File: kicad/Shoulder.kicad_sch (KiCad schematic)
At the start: 9 parts, among them U301 NSP4201MR6

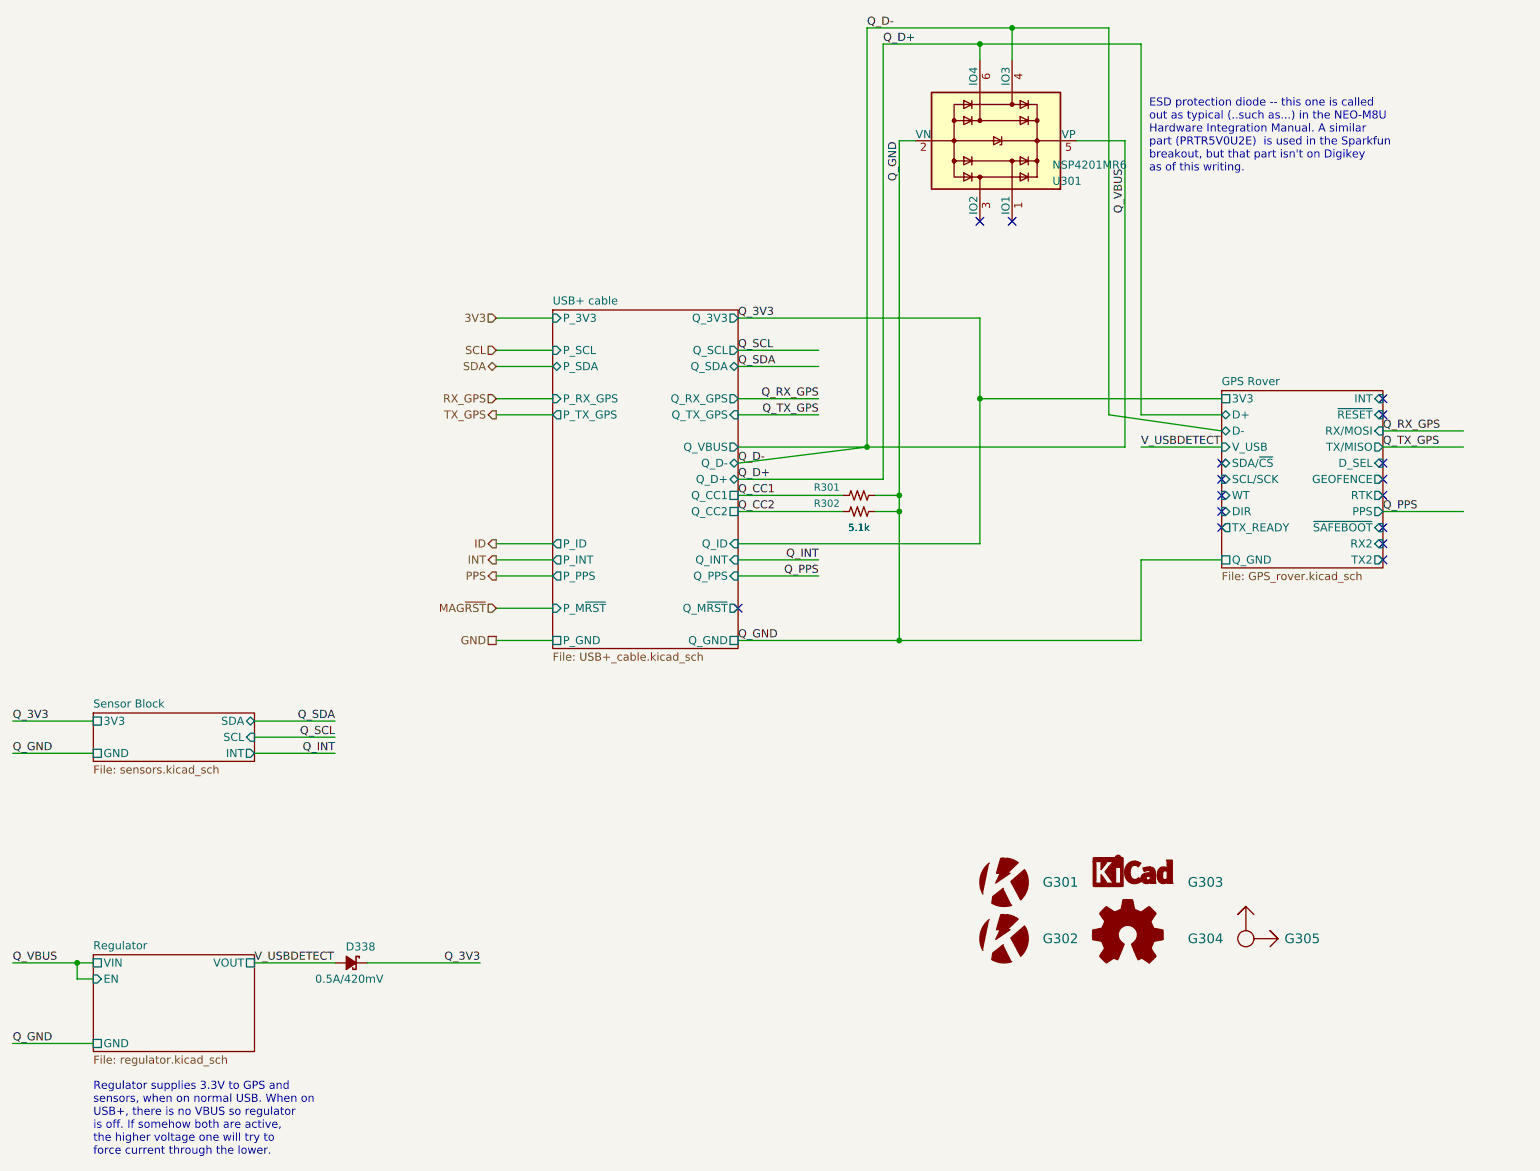
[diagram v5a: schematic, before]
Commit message: Corrected Digikey numbers
Stupid supply chain :( . Updated protection diode for data lines. Removed heirarchical pins which are no longer present in the nested sheet.
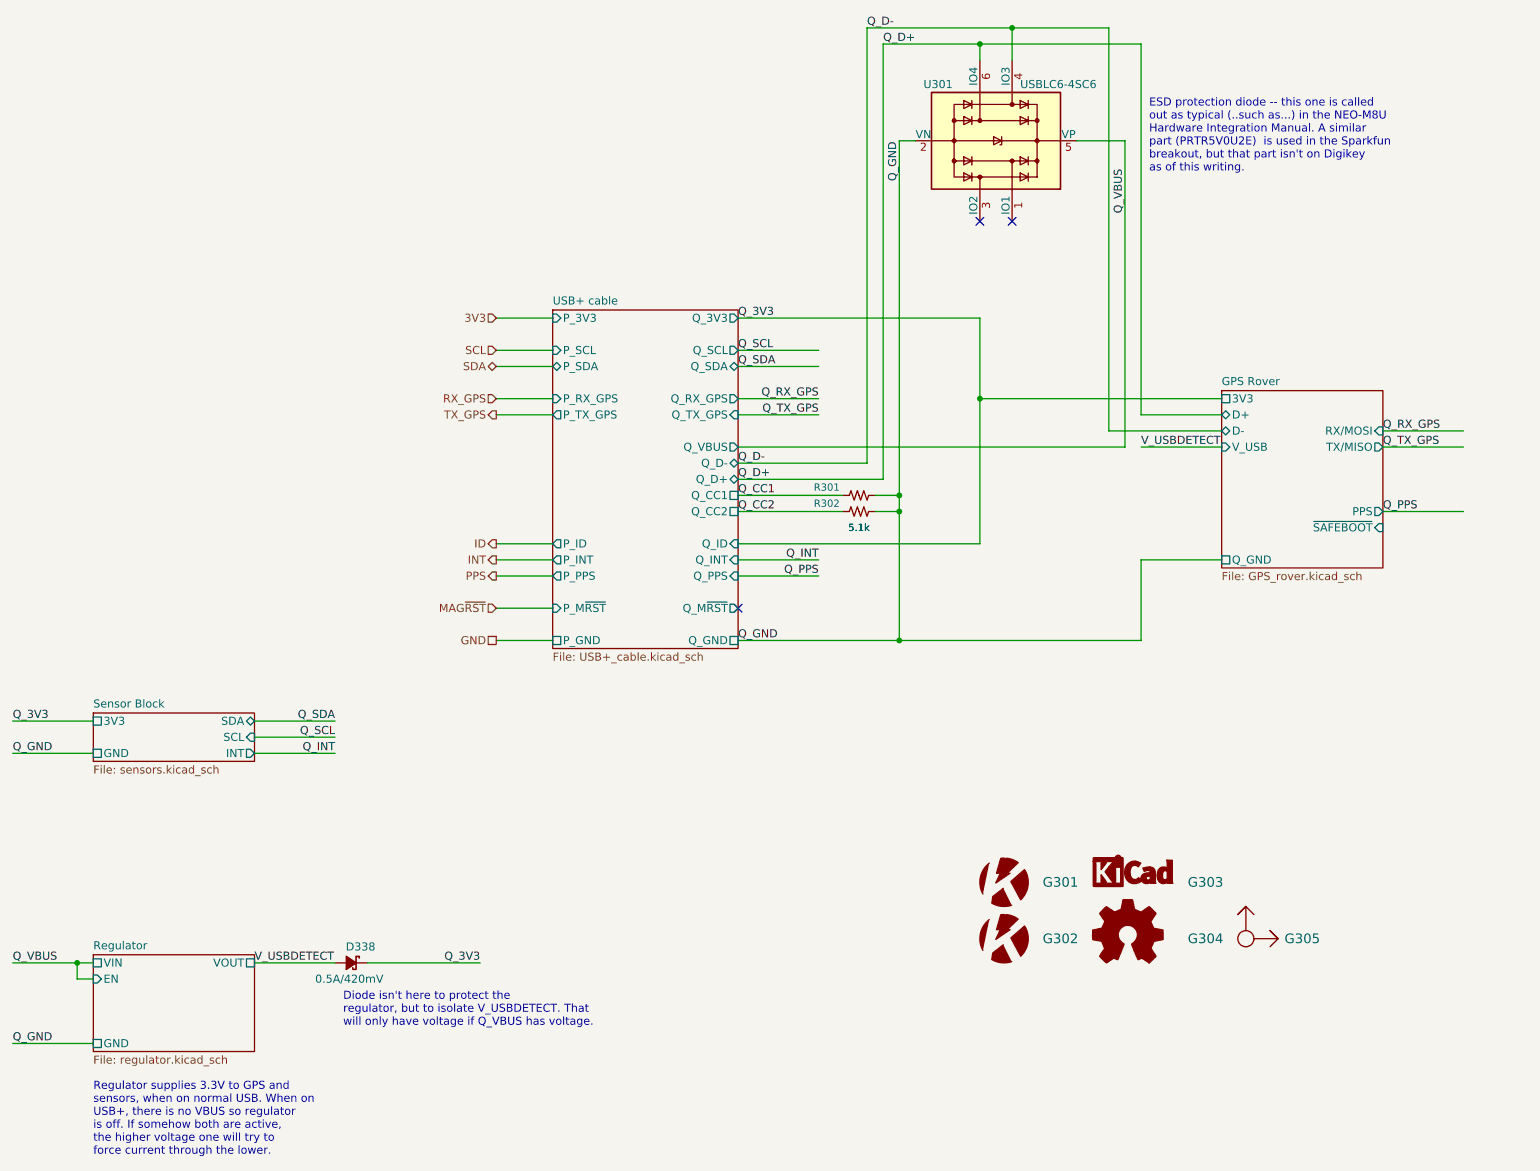
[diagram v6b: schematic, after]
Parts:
- D338: Digikey 641-1520-1-ND -> 641-1332-1-ND
- U301: value NSP4201MR6 -> USBLC6-4SC6; Digikey 497-5235-1-ND -> 497-4492-1-ND; Purpose USB DP protection diodes -> USB data ESD protection diodes
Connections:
- net Q_D-: no longer U301.5 (VP)
- new net Q_VBUS: U301.5 (VP)
- no-connect marks 16 -> 3
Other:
- sheet GPS Rover ports: added none; removed DIR, D_SEL, GEOFENCE, INT, RTK, RX2, SCL/SCK, SDA/~{CS}, TX2, TX_READY, WT, ~{RESET}
- note added: "Diode isn't here to protect the regulator, but to isolate V_USBDETECT. That will only have voltage if Q_VBUS has voltage."
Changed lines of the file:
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@@
   (junction (at 165.1 93.98) (diameter 0) (color 0 0 0 0)
   )
-  (junction (at 160.02 83.82) (diameter 0) (color 0 0 0 0)
-  )
   (junction (at 35.56 165.1) (diameter 0) (color 0 0 0 0)
   )
   (junction (at 165.1 91.44) (diameter 0) (color 0 0 0 0)
   )
-  (no_connect (at 215.9 96.52))
   (no_connect (at 182.88 48.26))
   (no_connect (at 139.7 109.22))
-  (no_connect (at 215.9 93.98))
-  (no_connect (at 215.9 91.44))
-  (no_connect (at 215.9 88.9))
-  (no_connect (at 215.9 86.36))
-  (no_connect (at 241.3 88.9))
-  (no_connect (at 241.3 91.44))
-  (no_connect (at 241.3 96.52))
-  (no_connect (at 241.3 99.06))
-  (no_connect (at 241.3 101.6))
-  (no_connect (at 241.3 86.36))
-  (no_connect (at 241.3 76.2))
-  (no_connect (at 241.3 78.74))
   (no_connect (at 177.8 48.26))
   (wire (pts (xy 241.3 83.82) (xy 254 83.82))
@@
     (stroke (width 0) (type default) (color 0 0 0 0))
   )
-  (wire (pts (xy 215.9 81.28) (xy 198.12 78.74))
+  (wire (pts (xy 198.12 17.78) (xy 198.12 81.28))
     (stroke (width 0) (type default) (color 0 0 0 0))
   )
@@
     (stroke (width 0) (type default) (color 0 0 0 0))
   )
+  (wire (pts (xy 139.7 86.36) (xy 160.02 86.36))
+    (stroke (width 0) (type default) (color 0 0 0 0))
+  )
   (wire (pts (xy 139.7 63.5) (xy 177.8 63.5))
     (stroke (width 0) (type default) (color 0 0 0 0))
   )
+  (wire (pts (xy 160.02 17.78) (xy 160.02 86.36))
+    (stroke (width 0) (type default) (color 0 0 0 0))
+  )
   (wire (pts (xy 177.8 76.2) (xy 215.9 76.2))
     (stroke (width 0) (type default) (color 0 0 0 0))
   )
-  (wire (pts (xy 139.7 83.82) (xy 160.02 83.82))
-    (stroke (width 0) (type default) (color 0 0 0 0))
-  )
   (wire (pts (xy 241.3 93.98) (xy 254 93.98))
     (stroke (width 0) (type default) (color 0 0 0 0))
@@
     (stroke (width 0) (type default) (color 0 0 0 0))
   )
-  (wire (pts (xy 160.02 83.82) (xy 200.66 83.82))
+  (wire (pts (xy 139.7 83.82) (xy 200.66 83.82))
     (stroke (width 0) (type default) (color 0 0 0 0))
   )
@@
     (stroke (width 0) (type default) (color 0 0 0 0))
   )
-  (wire (pts (xy 198.12 78.74) (xy 198.12 17.78))
-    (stroke (width 0) (type default) (color 0 0 0 0))
-  )
   (wire (pts (xy 160.02 17.78) (xy 182.88 17.78))
     (stroke (width 0) (type default) (color 0 0 0 0))
@@
     (stroke (width 0) (type default) (color 0 0 0 0))
   )
-  (wire (pts (xy 160.02 83.82) (xy 160.02 17.78))
-    (stroke (width 0) (type default) (color 0 0 0 0))
-  )
   (wire (pts (xy 203.2 20.32) (xy 203.2 78.74))
     (stroke (width 0) (type default) (color 0 0 0 0))
@@
     (stroke (width 0) (type default) (color 0 0 0 0))
   )
-  (wire (pts (xy 139.7 86.36) (xy 160.02 83.82))
-    (stroke (width 0) (type default) (color 0 0 0 0))
-  )
   (wire (pts (xy 177.8 20.32) (xy 203.2 20.32))
     (stroke (width 0) (type default) (color 0 0 0 0))
@@
   )
   (wire (pts (xy 182.88 17.78) (xy 182.88 22.86))
+    (stroke (width 0) (type default) (color 0 0 0 0))
+  )
+  (wire (pts (xy 215.9 81.28) (xy 198.12 81.28))
     (stroke (width 0) (type default) (color 0 0 0 0))
   )
@@
   (text "ESD protection diode -- this one is called\nout as typical (..such as...) in the NEO-M8U\nHardware Integration Manual. A similar\npart (PRTR5V0U2E)  is used in the Sparkfun\nbreakout, but that part isn't on Digikey\nas of this writing."
     (at 204.47 40.64 0)
+    (effects (font (size 1.27 1.27)) (justify left bottom))
+  )
+  (text "Diode isn't here to protect the\nregulator, but to isolate V_USBDETECT. That\nwill only have voltage if Q_VBUS has voltage."
+    (at 77.47 175.26 0)
     (effects (font (size 1.27 1.27)) (justify left bottom))
   )
@@
       (effects (font (size 1.27 1.27)) hide)
     )
-    (property "Digikey" "641-1520-1-ND" (id 4) (at 78.74 165.1 0)
+    (property "Digikey" "641-1332-1-ND" (id 4) (at 78.74 165.1 0)
       (effects (font (size 1.27 1.27)) hide)
     )
@@
   (symbol (lib_id "Power_Protection:SRV05-4") (at 180.34 35.56 270) (mirror x) (unit 1)
     (in_bom yes) (on_board yes)
-    (property "Reference" "U301" (id 0) (at 189.23 41.91 90)
-      (effects (font (size 1.27 1.27)) (justify left))
-    )
-    (property "Value" "NSP4201MR6" (id 1) (at 189.23 39.37 90)
+    (property "Reference" "U301" (id 0) (at 168.91 26.67 90)
+      (effects (font (size 1.27 1.27)) (justify left))
+    )
+    (property "Value" "USBLC6-4SC6" (id 1) (at 184.15 26.67 90)
       (effects (font (size 1.27 1.27)) (justify left))
     )
@@
       (effects (font (size 1.27 1.27)) hide)
     )
-    (property "Digikey" "497-5235-1-ND" (id 4) (at 180.34 35.56 0)
-      (effects (font (size 1.27 1.27)) hide)
-    )
-    (property "Purpose" "USB DP protection diodes" (id 5) (at 180.34 35.56 0)
+    (property "Digikey" "497-4492-1-ND" (id 4) (at 180.34 35.56 0)
+      (effects (font (size 1.27 1.27)) hide)
+    )
+    (property "Purpose" "USB data ESD protection diodes" (id 5) (at 180.34 35.56 0)
       (effects (font (size 1.27 1.27)) hide)
     )
@@
       (effects (font (size 1.27 1.27)) (justify left))
     )
-    (pin "WT" input (at 215.9 91.44 180)
-      (effects (font (size 1.27 1.27)) (justify left))
-    )
-    (pin "DIR" input (at 215.9 93.98 180)
-      (effects (font (size 1.27 1.27)) (justify left))
-    )
     (pin "D-" bidirectional (at 215.9 81.28 180)
       (effects (font (size 1.27 1.27)) (justify left))
@@
     (pin "3V3" passive (at 215.9 76.2 180)
       (effects (font (size 1.27 1.27)) (justify left))
-    )
-    (pin "GEOFENCE" output (at 241.3 88.9 0)
-      (effects (font (size 1.27 1.27)) (justify right))
-    )
-    (pin "RTK" output (at 241.3 91.44 0)
-      (effects (font (size 1.27 1.27)) (justify right))
     )
     (pin "PPS" output (at 241.3 93.98 0)
@@
       (effects (font (size 1.27 1.27)) (justify right))
     )
-    (pin "RX2" input (at 241.3 99.06 0)
-      (effects (font (size 1.27 1.27)) (justify right))
-    )
     (pin "Q_GND" passive (at 215.9 101.6 180)
       (effects (font (size 1.27 1.27)) (justify left))
-    )
-    (pin "D_SEL" input (at 241.3 86.36 0)
-      (effects (font (size 1.27 1.27)) (justify right))
-    )
-    (pin "TX2" output (at 241.3 101.6 0)
-      (effects (font (size 1.27 1.27)) (justify right))
     )
     (pin "TX{slash}MISO" output (at 241.3 83.82 0)
@@
       (effects (font (size 1.27 1.27)) (justify right))
     )
-    (pin "~{RESET}" input (at 241.3 78.74 0)
-      (effects (font (size 1.27 1.27)) (justify right))
-    )
-    (pin "INT" input (at 241.3 76.2 0)
-      (effects (font (size 1.27 1.27)) (justify right))
-    )
-    (pin "SDA{slash}~{CS}" bidirectional (at 215.9 86.36 180)
-      (effects (font (size 1.27 1.27)) (justify left))
-    )
-    (pin "SCL{slash}SCK" input (at 215.9 88.9 180)
-      (effects (font (size 1.27 1.27)) (justify left))
-    )
-    (pin "TX_READY" output (at 215.9 96.52 180)
-      (effects (font (size 1.27 1.27)) (justify left))
-    )
     (pin "V_USB" input (at 215.9 83.82 180)
